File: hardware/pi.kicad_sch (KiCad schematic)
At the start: 59 parts, among them SW1 BOOTSEL, SW2 RESET, U10 RP2040, U11 SS54_C22452, U12 SS54_C22452, U13 CAN_IO, U14 TJA1042T_3_1J, U15 USB-C, U5 AMS1117-3_3_C347222, U6 SKCR-16S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

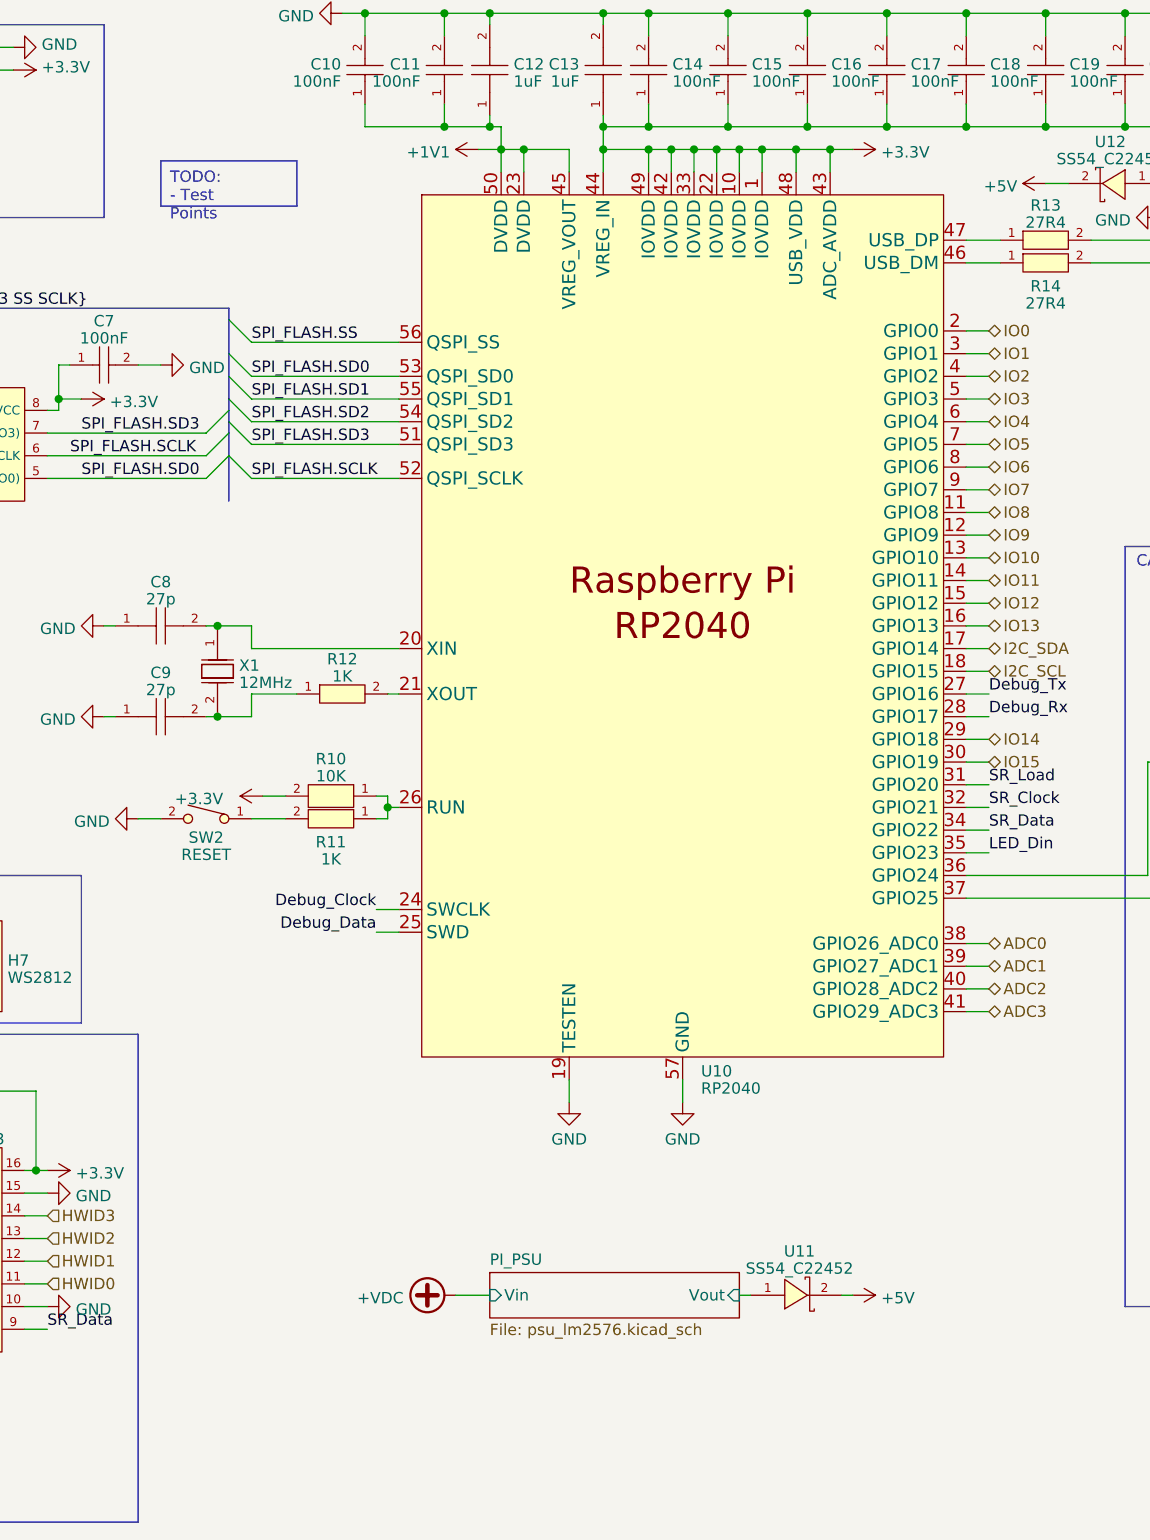
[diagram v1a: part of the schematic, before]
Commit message: fuse for main 5v. parts moved and made dimensions smaller.
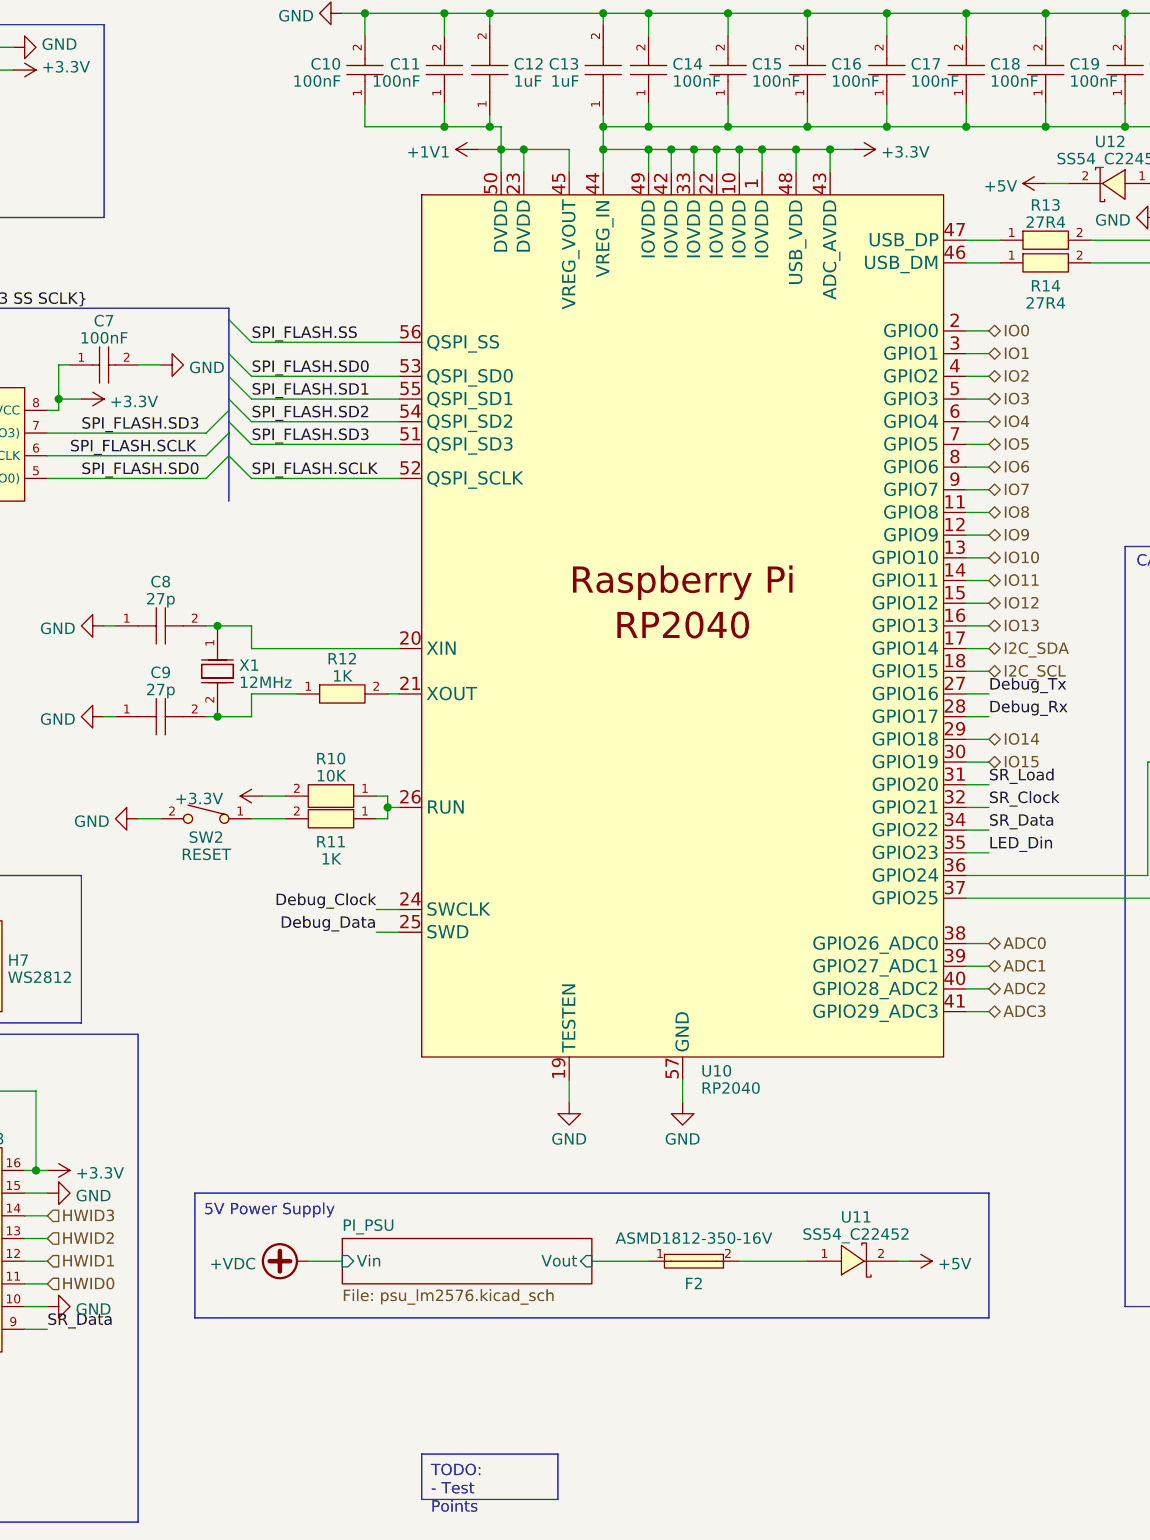
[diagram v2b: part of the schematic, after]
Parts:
- added F2: ASMD1812-350-16V, jlc_footprints:F1812, symbol jlc:ASMD1812-350-16V
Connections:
- net PI_PSU/Vout: now also F2.1; no longer U11.1 (A)
- new net: F2.2, U11.1 (A)
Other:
- moved on the sheet: U11
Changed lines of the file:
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@@
     (stroke (width 0) (type default))
   )
+  (wire (pts (xy 137.16 154.94) (xy 143.51 154.94))
+    (stroke (width 0) (type default))
+  )
   (wire (pts (xy 55.88 24.13) (xy 57.15 24.13))
     (stroke (width 0) (type default))
@@
     (stroke (width 0) (type default))
   )
-  (wire (pts (xy 153.67 158.75) (xy 154.94 158.75))
-    (stroke (width 0) (type default))
-  )
   (wire (pts (xy 205.74 15.24) (xy 205.74 17.78))
     (stroke (width 0) (type default))
@@
     (stroke (width 0) (type default))
   )
-  (wire (pts (xy 121.92 158.75) (xy 125.73 158.75))
+  (wire (pts (xy 105.41 154.94) (xy 109.22 154.94))
     (stroke (width 0) (type default))
   )
@@
     (stroke (width 0) (type default))
   )
+  (wire (pts (xy 153.67 154.94) (xy 161.29 154.94))
+    (stroke (width 0) (type default))
+  )
   (wire (pts (xy 151.13 30.48) (xy 151.13 33.02))
     (stroke (width 0) (type default))
@@
     (stroke (width 0) (type default))
   )
-  (wire (pts (xy 165.1 158.75) (xy 166.37 158.75))
+  (wire (pts (xy 171.45 154.94) (xy 172.72 154.94))
     (stroke (width 0) (type default))
   )
@@
   )
   (text_box "TODO:\n- Test Points"
-    (at 88.9 31.75 0) (size 15.24 5.08)
+    (at 118.11 176.53 0) (size 15.24 5.08)
+    (stroke (width 0) (type default))
+    (fill (type none))
+    (effects (font (size 1.27 1.27)) (justify left top))
+  )
+  (text_box "5V Power Supply"
+    (at 92.71 147.32 0) (size 88.9 13.97)
     (stroke (width 0) (type default))
     (fill (type none))
@@
     )
   )
+  (symbol (lib_id "jlc:ASMD1812-350-16V") (at 148.59 154.94 0) (unit 1)
+    (in_bom yes) (on_board yes) (dnp no)
+    (property "Reference" "F2" (at 148.59 157.48 0)
+      (effects (font (size 1.27 1.27)))
+    )
+    (property "Value" "ASMD1812-350-16V" (at 148.59 152.4 0)
+      (effects (font (size 1.27 1.27)))
+    )
+    (property "Footprint" "jlc_footprints:F1812" (at 148.59 165.1 0)
+      (effects (font (size 1.27 1.27) italic) hide)
+    )
+    (property "Datasheet" "https://item.szlcsc.com/343302.html" (at 146.304 154.813 0)
+      (effects (font (size 1.27 1.27)) (justify left) hide)
+    )
+    (property "LCSC" "C2982285" (at 148.59 154.94 0)
+      (effects (font (size 1.27 1.27)) hide)
+    )
+    (pin "1")
+    (pin "2")
+    (instances
+      (project "dispensy"
+        (path "/a50b51f9-900f-4bbb-8934-4acbc429c37b/f8ce2893-59d6-4502-b3c7-412c7467c1ef"
+          (reference "F2") (unit 1)
+        )
+      )
+    )
+  )
   (symbol (lib_id "jlc:AMS1117-3_3_C347222") (at 33.02 29.21 0) (mirror y) (unit 1)
     (in_bom yes) (on_board yes) (dnp no)
@@
     )
   )
-  (symbol (lib_id "power:+5V") (at 166.37 158.75 270) (unit 1)
+  (symbol (lib_id "power:+5V") (at 172.72 154.94 270) (unit 1)
     (in_bom yes) (on_board yes) (dnp no) (fields_autoplaced)
-    (property "Reference" "#PWR056" (at 162.56 158.75 0)
+    (property "Reference" "#PWR056" (at 168.91 154.94 0)
       (effects (font (size 1.27 1.27)) hide)
     )
-    (property "Value" "+5V" (at 169.545 159.0668 90)
+    (property "Value" "+5V" (at 175.895 155.2568 90)
       (effects (font (size 1.27 1.27)) (justify left))
     )
-    (property "Footprint" "" (at 166.37 158.75 0)
+    (property "Footprint" "" (at 172.72 154.94 0)
       (effects (font (size 1.27 1.27)) hide)
     )
-    (property "Datasheet" "" (at 166.37 158.75 0)
+    (property "Datasheet" "" (at 172.72 154.94 0)
       (effects (font (size 1.27 1.27)) hide)
     )
@@
     )
   )
-  (symbol (lib_id "power:+VDC") (at 121.92 158.75 90) (unit 1)
+  (symbol (lib_id "power:+VDC") (at 105.41 154.94 90) (unit 1)
     (in_bom yes) (on_board yes) (dnp no) (fields_autoplaced)
-    (property "Reference" "#PWR051" (at 124.46 158.75 0)
+    (property "Reference" "#PWR051" (at 107.95 154.94 0)
       (effects (font (size 1.27 1.27)) hide)
     )
-    (property "Value" "+VDC" (at 116.078 159.0668 90)
+    (property "Value" "+VDC" (at 99.568 155.2568 90)
       (effects (font (size 1.27 1.27)) (justify left))
     )
-    (property "Footprint" "" (at 121.92 158.75 0)
+    (property "Footprint" "" (at 105.41 154.94 0)
       (effects (font (size 1.27 1.27)) hide)
     )
-    (property "Datasheet" "" (at 121.92 158.75 0)
+    (property "Datasheet" "" (at 105.41 154.94 0)
       (effects (font (size 1.27 1.27)) hide)
     )
@@
     )
   )
-  (symbol (lib_id "jlc:SS54_C22452") (at 160.02 158.75 180) (unit 1)
+  (symbol (lib_id "jlc:SS54_C22452") (at 166.37 154.94 180) (unit 1)
     (in_bom yes) (on_board yes) (dnp no) (fields_autoplaced)
-    (property "Reference" "U11" (at 160.401 153.8351 0)
+    (property "Reference" "U11" (at 166.751 150.0251 0)
       (effects (font (size 1.27 1.27)))
     )
-    (property "Value" "SS54_C22452" (at 160.401 155.7561 0)
+    (property "Value" "SS54_C22452" (at 166.751 151.9461 0)
       (effects (font (size 1.27 1.27)))
     )
-    (property "Footprint" "jlc_footprints:SMA_L4.4-W2.8-LS5.4-R-RD" (at 160.02 148.59 0)
+    (property "Footprint" "jlc_footprints:SMA_L4.4-W2.8-LS5.4-R-RD" (at 166.37 144.78 0)
       (effects (font (size 1.27 1.27) italic) hide)
     )
-    (property "Datasheet" "https://item.szlcsc.com/310096.html" (at 162.306 158.877 0)
+    (property "Datasheet" "https://item.szlcsc.com/310096.html" (at 168.656 155.067 0)
       (effects (font (size 1.27 1.27)) (justify left) hide)
     )
-    (property "LCSC" "C22452" (at 160.02 158.75 0)
+    (property "LCSC" "C22452" (at 166.37 154.94 0)
       (effects (font (size 1.27 1.27)) hide)
     )
@@
     )
   )
-  (sheet (at 125.73 156.21) (size 27.94 5.08) (fields_autoplaced)
+  (sheet (at 109.22 152.4) (size 27.94 5.08) (fields_autoplaced)
     (stroke (width 0.1524) (type solid))
     (fill (color 0 0 0 0.0000))
-    (property "Sheetname" "PI_PSU" (at 125.73 155.4984 0)
+    (property "Sheetname" "PI_PSU" (at 109.22 151.6884 0)
       (effects (font (size 1.27 1.27)) (justify left bottom))
     )
-    (property "Sheetfile" "psu_lm2576.kicad_sch" (at 125.73 161.8746 0)
+    (property "Sheetfile" "psu_lm2576.kicad_sch" (at 109.22 158.0646 0)
       (effects (font (size 1.27 1.27)) (justify left top))
     )
-    (pin "Vin" input (at 125.73 158.75 180)
+    (pin "Vin" input (at 109.22 154.94 180)
       (effects (font (size 1.27 1.27)) (justify left))
     )
-    (pin "Vout" input (at 153.67 158.75 0)
+    (pin "Vout" input (at 137.16 154.94 0)
       (effects (font (size 1.27 1.27)) (justify right))
     )

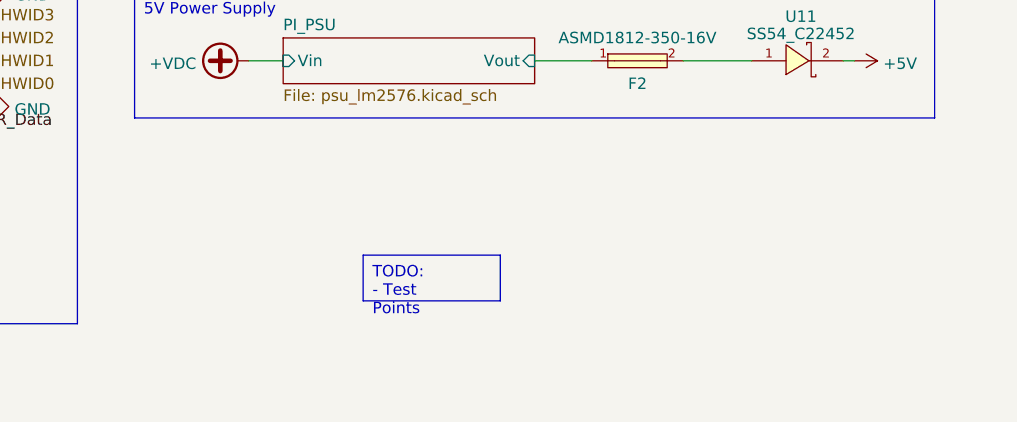
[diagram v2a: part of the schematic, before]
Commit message: add power status leds
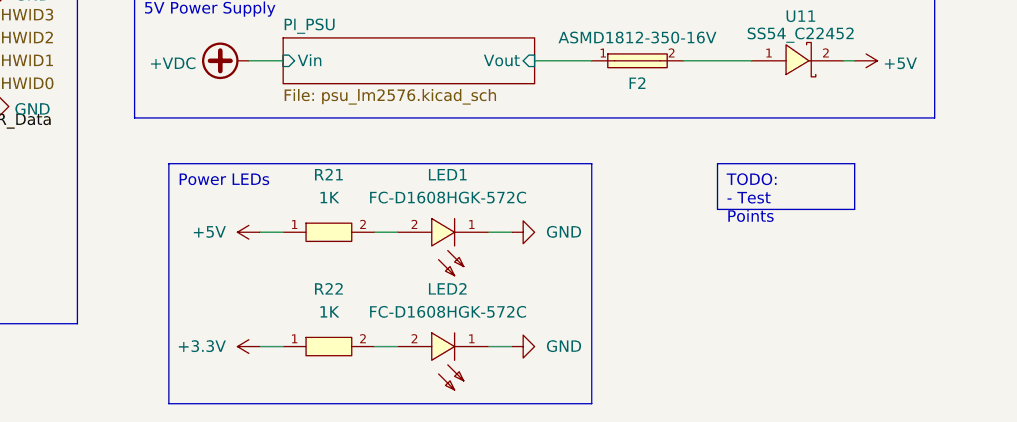
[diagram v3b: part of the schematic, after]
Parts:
- added LED1, LED2: FC-D1608HGK-572C, jlc_footprints:LED0603-RD, symbol jlc:FC-D1608HGK-572C
- added R21, R22: 1K, jlc_footprints:R0402, symbol jlc:CR-02FL6----1K
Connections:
- net +3.3V: now also R22.1
- net +5V: now also R21.1
- net GND: now also LED1.1 (-), LED2.1 (-)
- new net: LED2.2 (+), R22.2
- new net: LED1.2 (+), R21.2

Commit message: replace rgb led connector with screw terminal
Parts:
- removed H7: WS2812, jlc_footprints:HDR-TH_3P-P2.54-V-F, symbol jlc:22025403P00CKMT
- added H7: WS2812, jlc_footprints:CONN-TH_XY300V-A-5.0-3P, symbol jlc:XY300V-A-5_0-3P
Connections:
- net +5V: now also H7.3
- net GND: now also H7.1
- net at U7.2 (DO): now also H7.2
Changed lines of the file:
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@@
 	(title_block
 		(title "Pi RP2040 MCU")
-		(date "2024-02-05")
+		(date "2024-04-06")
 		(rev "1")
 		(company "DrinkRobotics")
@@
 		)
 	)
-	(text_box "TODO:\n- Test Points"
-		(exclude_from_sim no)
-		(at 157.48 166.37 0)
-		(size 15.24 5.08)
-		(stroke
-			(width 0)
-			(type default)
-		)
-		(fill
-			(type none)
-		)
-		(effects
-			(font
-				(size 1.27 1.27)
-			)
-			(justify left top)
-		)
-	)
 	(text_box "5V Power Supply"
 		(exclude_from_sim no)
@@
 	)
 	(symbol
-		(lib_id "jlc:22025403P00CKMT")
-		(at 67.31 121.92 0)
-		(unit 1)
-		(exclude_from_sim no)
-		(in_bom yes)
-		(on_board yes)
-		(dnp no)
-		(fields_autoplaced yes)
-		(property "Reference" "H7"
-			(at 71.755 121.2763 0)
-			(effects
-				(font
-					(size 1.27 1.27)
-				)
-				(justify left)
-			)
-		)
-		(property "Value" "WS2812"
-			(at 71.755 123.1973 0)
-			(effects
-				(font
-					(size 1.27 1.27)
-				)
-				(justify left)
-			)
-		)
-		(property "Footprint" "jlc_footprints:HDR-TH_3P-P2.54-V-F"
-			(at 67.31 132.08 0)
-			(effects
-				(font
-					(size 1.27 1.27)
-					(italic yes)
-				)
-				(hide yes)
-			)
-		)
-		(property "Datasheet" "https://item.szlcsc.com/562471.html"
-			(at 65.024 121.793 0)
-			(effects
-				(font
-					(size 1.27 1.27)
-				)
-				(justify left)
-				(hide yes)
-			)
-		)
-		(property "Description" ""
-			(at 67.31 121.92 0)
-			(effects
-				(font
-					(size 1.27 1.27)
-				)
-				(hide yes)
-			)
-		)
-		(property "LCSC" "C146690"
-			(at 67.31 121.92 0)
-			(effects
-				(font
-					(size 1.27 1.27)
-				)
-				(hide yes)
-			)
-		)
-		(pin "1"
-		)
-		(pin "2"
-		)
-		(pin "3"
-		)
-		(instances
-			(project "dispensy"
-				(path "/a50b51f9-900f-4bbb-8934-4acbc429c37b/f8ce2893-59d6-4502-b3c7-412c7467c1ef"
-					(reference "H7")
-					(unit 1)
-				)
-			)
-		)
-	)
-	(symbol
 		(lib_id "power:GND")
 		(at 88.9 54.61 90)
@@
 					(unit 1)
 				)
+			)
+		)
+	)
+	(symbol
+		(lib_id "jlc:XY300V-A-5_0-3P")
+		(at 68.58 121.92 0)
+		(unit 1)
+		(exclude_from_sim no)
+		(in_bom yes)
+		(on_board yes)
+		(dnp no)
+		(fields_autoplaced yes)
+		(property "Reference" "H7"
+			(at 71.755 120.7078 0)
+			(effects
+				(font
+					(size 1.27 1.27)
+				)
+				(justify left)
+			)
+		)
+		(property "Value" "WS2812"
+			(at 71.755 123.1321 0)
+			(effects
+				(font
+					(size 1.27 1.27)
+				)
+				(justify left)
+			)
+		)
+		(property "Footprint" "jlc_footprints:CONN-TH_XY300V-A-5.0-3P"
+			(at 68.58 132.08 0)
+			(effects
+				(font
+					(size 1.27 1.27)
+					(italic yes)
+				)
+				(hide yes)
+			)
+		)
+		(property "Datasheet" "https://item.szlcsc.com/943867.html?ref=editor&logined=true"
+			(at 66.294 121.793 0)
+			(effects
+				(font
+					(size 1.27 1.27)
+				)
+				(justify left)
+				(hide yes)
+			)
+		)
+		(property "Description" ""
+			(at 68.58 121.92 0)
+			(effects
+				(font
+					(size 1.27 1.27)
+				)
+				(hide yes)
+			)
+		)
+		(property "LCSC" "C880594"
+			(at 68.58 121.92 0)
+			(effects
+				(font
+					(size 1.27 1.27)
+				)
+				(hide yes)
+			)
+		)
+		(pin "3"
+		)
+		(pin "1"
+		)
+		(pin "2"
+		)
+		(instances
+			(project "dispensy"
+				(path "/a50b51f9-900f-4bbb-8934-4acbc429c37b/f8ce2893-59d6-4502-b3c7-412c7467c1ef"
+					(reference "H7")
+					(unit 1)
+				)
